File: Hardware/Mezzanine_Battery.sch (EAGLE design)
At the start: 22 parts, among them U1 MCP73831, U2 EDISON_CONNECTOR_FULLMOUNTING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, U3 EDISON_CONNECTOR_FULLHEADER

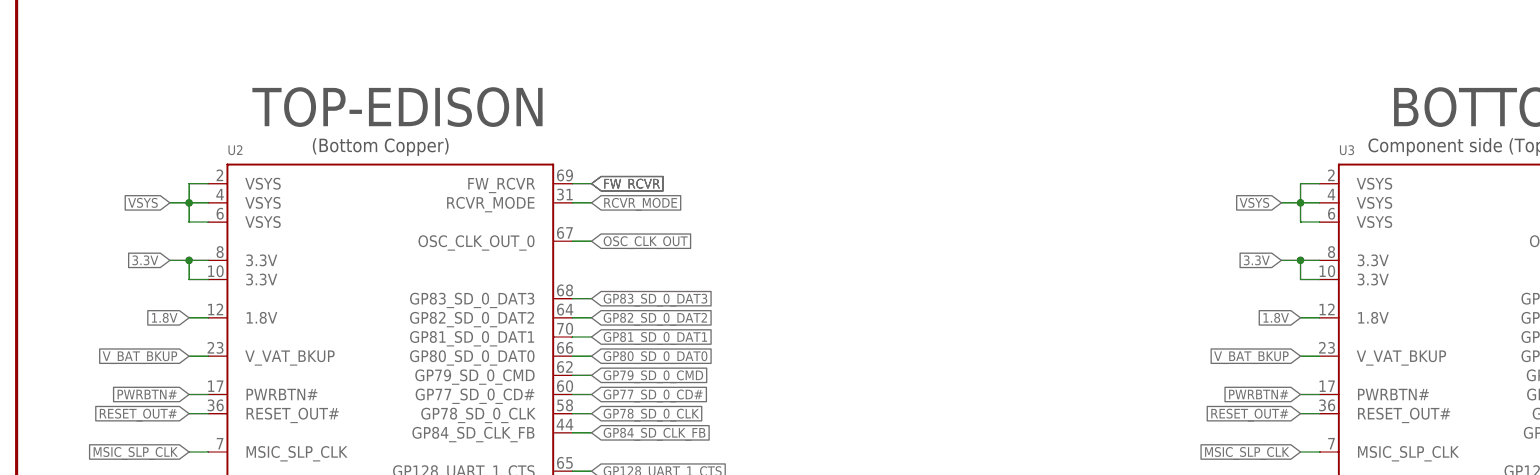
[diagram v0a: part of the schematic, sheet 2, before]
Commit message: corrected names, added DCIN, cleaned up dimensions
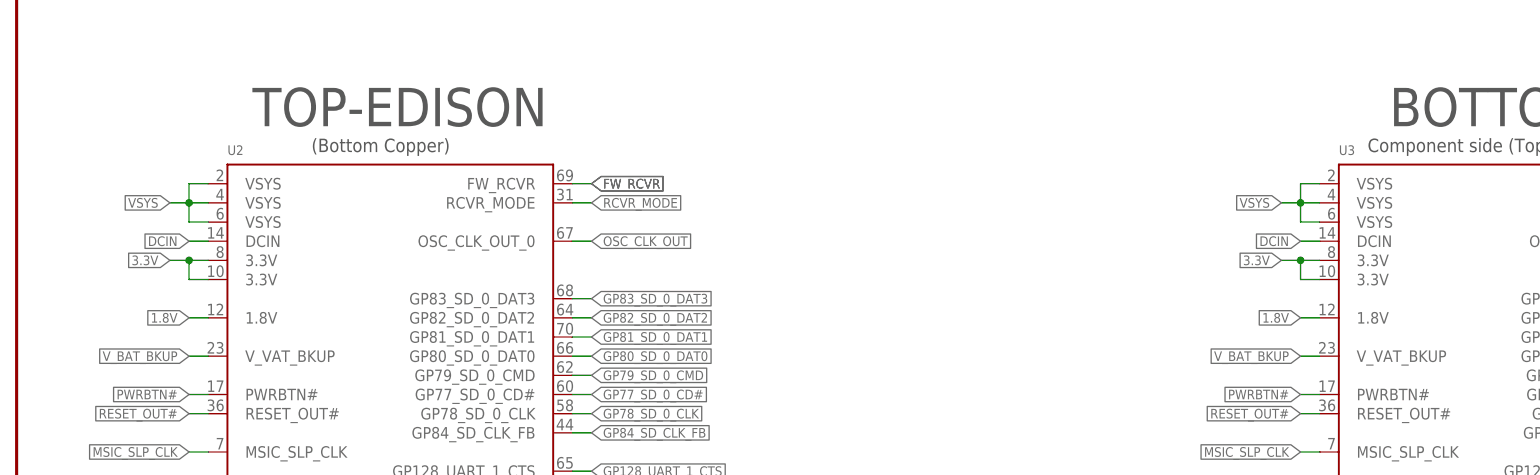
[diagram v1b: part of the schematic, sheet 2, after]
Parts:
- JP1: value USB_MICROB_PLUGCONN-11752 -> USB_MICROB_PLUG
- SJ1: value JUMPER-PAD-2-NC_BY_TRACE -> LED DISABLE
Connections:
- new net DCIN: U2.DCIN, U3.DCIN
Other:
- note added: "v02"
- note removed: "v01"
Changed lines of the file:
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@@
 <part name="FID1" library="SparkFun-Aesthetics" deviceset="FIDUCIAL" device="1X2"/>
 <part name="FID2" library="SparkFun-Aesthetics" deviceset="FIDUCIAL" device="1X2"/>
-<part name="JP1" library="SparkFun-Connectors" deviceset="USB_MICROB_PLUG" device="CONN-11752"/>
+<part name="JP1" library="SparkFun-Connectors" deviceset="USB_MICROB_PLUG" device="CONN-11752" value="USB_MICROB_PLUG"/>
 <part name="GND1" library="SparkFun-Aesthetics" deviceset="GND" device=""/>
 <part name="GND2" library="SparkFun-Aesthetics" deviceset="GND" device=""/>
@@
 <part name="R3" library="SparkFun-Resistors" deviceset="1KOHM1/10W1%(0603)" device="" value="1k"/>
 <part name="GND9" library="SparkFun-Aesthetics" deviceset="GND" device=""/>
-<part name="SJ1" library="SparkFun-Passives" deviceset="JUMPER-PAD-2-NC_BY_TRACE" device=""/>
+<part name="SJ1" library="SparkFun-Passives" deviceset="JUMPER-PAD-2-NC_BY_TRACE" device="" value="LED DISABLE"/>
 <part name="FID3" library="SparkFun-Aesthetics" deviceset="FIDUCIAL" device="1X2"/>
 <part name="FID4" library="SparkFun-Aesthetics" deviceset="FIDUCIAL" device="1X2"/>
@@
 <plain>
 <text x="167.64" y="10.16" size="2.54" layer="94">Casey Kuhns</text>
-<text x="238.76" y="7.62" size="2.54" layer="94">v01</text>
+<text x="238.76" y="7.62" size="2.54" layer="94">v02</text>
 </plain>
 <instances>
@@
 </segment>
 </net>
+<net name="DCIN" class="0">
+<segment>
+<pinref part="U3" gate="G$1" pin="DCIN"/>
+<wire x1="172.72" y1="152.4" x2="170.18" y2="152.4" width="0.1524" layer="91"/>
+<label x="170.18" y="152.4" size="1.27" layer="95" rot="R180" xref="yes"/>
+</segment>
+<segment>
+<pinref part="U2" gate="G$1" pin="DCIN"/>
+<wire x1="25.4" y1="152.4" x2="22.86" y2="152.4" width="0.1524" layer="91"/>
+<label x="22.86" y="152.4" size="1.27" layer="95" rot="R180" xref="yes"/>
+</segment>
+</net>
